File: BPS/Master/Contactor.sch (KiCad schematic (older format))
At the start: 20 parts, among them J7 ContactorConnector, Q1 VND5N07-E, Q2 NTR4003NT1G, U10 BAS70-04, U11 SI8261ABC-IS

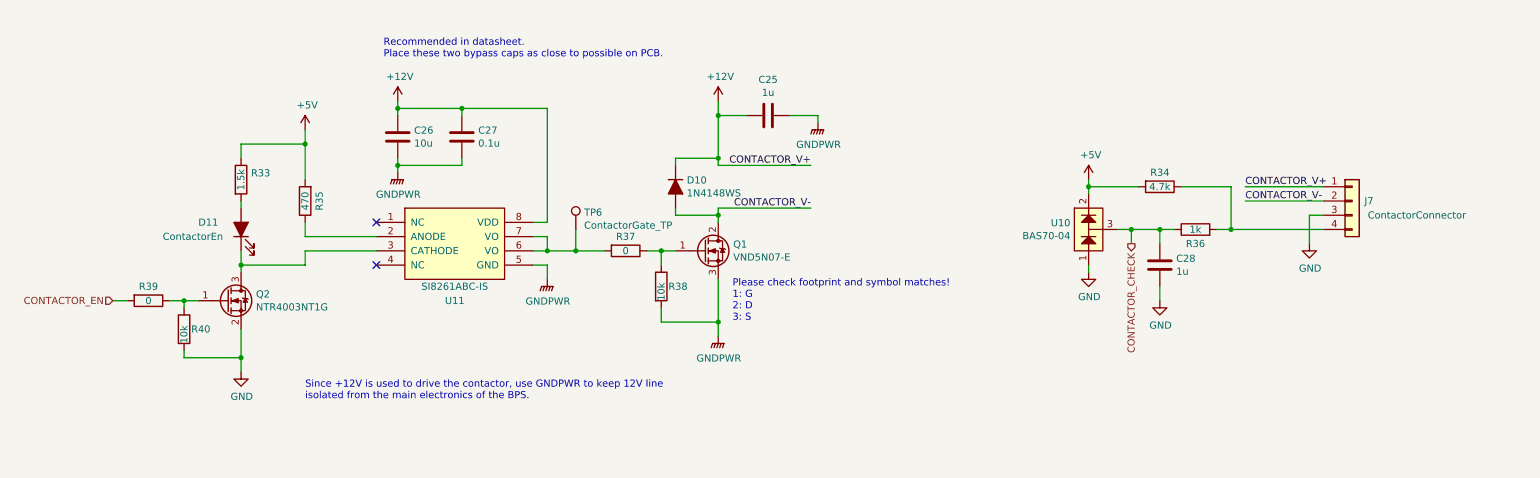
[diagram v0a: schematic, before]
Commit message: Creates fan brd interface schematics and updates symbols/footprints related to the leader board
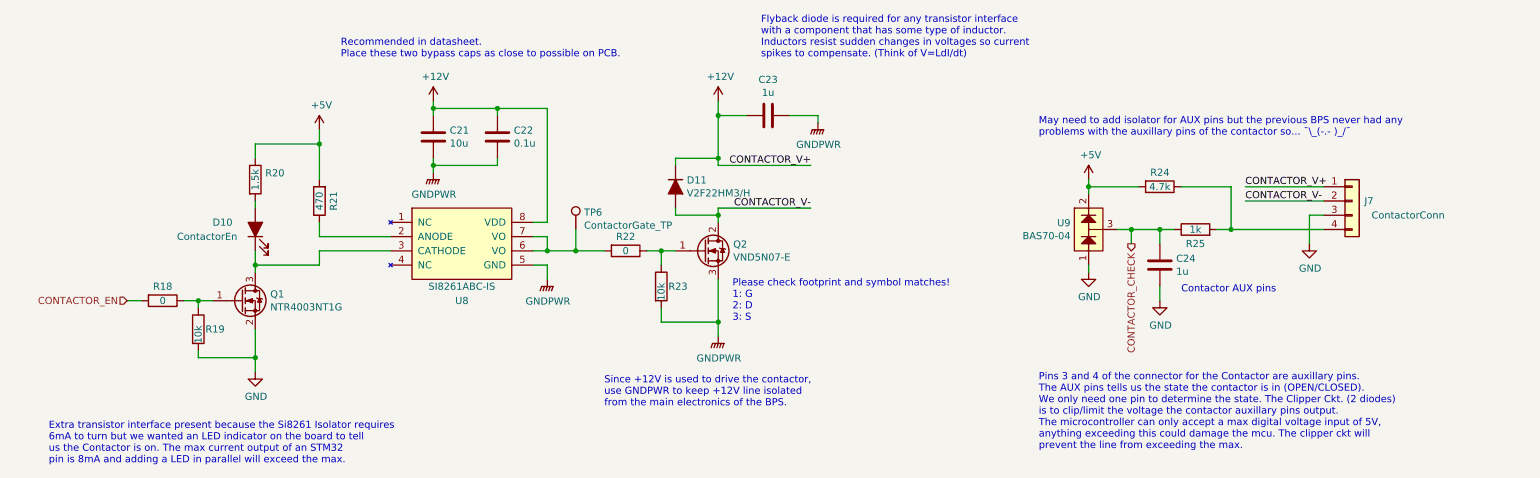
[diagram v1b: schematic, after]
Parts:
- removed U10: BAS70-04, Package_TO_SOT_SMD:SOT-23, symbol BPSMaster-rescue:BAS70-04-utsvt-bps
- removed U11: SI8261ABC-IS, Package_SO:SOIC-8_3.9x4.9mm_P1.27mm, symbol BPSMaster-rescue:SI8261ABC-IS-utsvt-bps
- added U8: SI8261ABC-IS, Package_SO:SOIC-8_3.9x4.9mm_P1.27mm, symbol utsvt-bps:SI8261ABC-IS
- added U9: BAS70-04, Package_TO_SOT_SMD:SOT-23, symbol utsvt-bps:BAS70-04
- D11: renamed from D10; value 1N4148WS -> V2F22HM3/H; footprint Diode_SMD:D_SOD-323 -> UTSVT_Passive:V2F22HM; Mouser (none) -> https://www.mouser.com/ProductDetail/Vishay-Semiconductors/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
- J7: value ContactorConnector -> ContactorConn
- renumbered C26 to C21, C27 to C22, C25 to C23, C28 to C24, D11 to D10, Q2 to Q1, Q1 to Q2, R39 to R18, R40 to R19, R33 to R20, R35 to R21, R37 to R22, R38 to R23, R34 to R24, R36 to R25
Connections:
- net +12V: now also U8.8 (VDD)
- net +5V: now also U9.2
- net CONTACTOR_CHECK: now also U9.3
- net GND: now also U9.1
- net GNDPWR: now also U8.5 (GND)
- net at R22.2, TP6.1: now also U8.6 (VO), U8.7 (VO)
- net at R21.1: now also U8.2 (ANODE)
- net at D10.1 (K), Q1.3 (D): now also U8.3 (CATHODE)
- no-connect marks 2 -> 0
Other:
- note added: "Contactor AUX pins"
- note added: "Extra transistor interface present because the Si8261 Isolator requires\n6mA to turn but we wanted an LED indicator on the board to tell\nus the Contactor is on. The max current output of an STM32\npin is 8mA and adding a LED in parallel will exceed the max."
- note added: "Flyback diode is required for any transistor interface\nwith a component that has some type of inductor.\nInductors resist sudden changes in voltages so current\nspikes to compensate. (Think of V=LdI/dt)"
- note added: "May need to add isolator for AUX pins but the previous BPS never had any\nproblems with the auxillary pins of the contactor so... ¯\_(-.- )_/¯"
- note added: "Pins 3 and 4 of the connector for the Contactor are auxillary pins.\nThe AUX pins tells us the state the contactor is in (OPEN/CLOSED).\nWe only need one pin to determine the state. The Clipper Ckt. (2 diodes)\nis to clip/limit the voltage the contactor auxillary pins output.\nThe microcontroller can only accept a max digital voltage input of 5V,\nanything exceeding this could damage the mcu. The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"
- note added: "Since +12V is used to drive the contactor,\nuse GNDPWR to keep +12V line isolated\nfrom the main electronics of the BPS."
- note removed: "Since +12V is used to drive the contactor, use GNDPWR to keep 12V line\nisolated from the main electronics of the BPS."
- moved on the sheet: C21, C22, D10, Q1, R18, R19, R20, R21

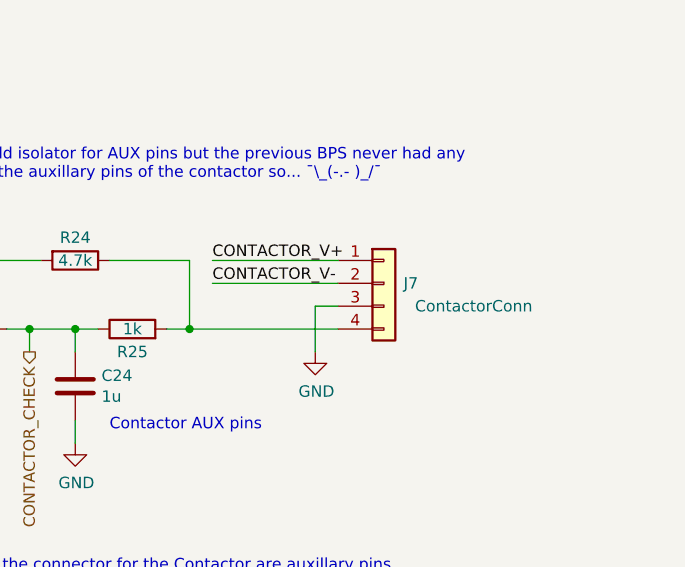
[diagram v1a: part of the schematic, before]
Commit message: Finishes schematics for bps leader board
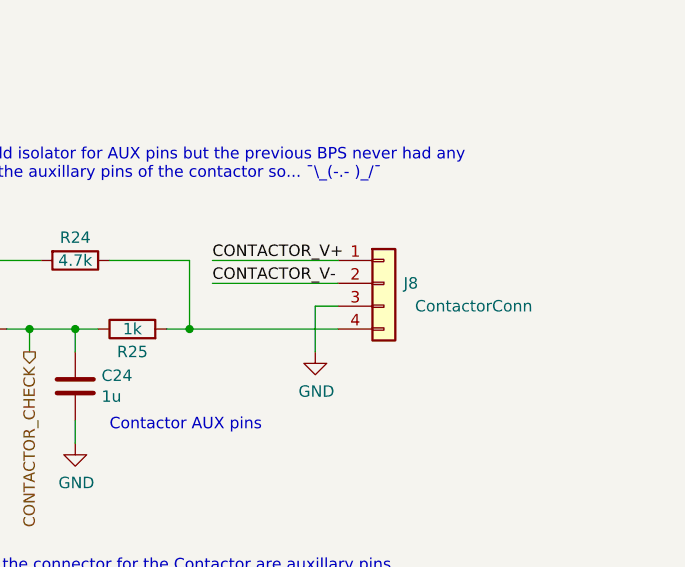
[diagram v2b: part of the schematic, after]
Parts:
- renumbered J7 to J8
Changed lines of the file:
@@
 $Descr A4 11693 8268
 encoding utf-8
-Sheet 6 10
+Sheet 6 11
 Title ""
 Date ""
@@
 $EndDescr
 $Comp
-L Connector_Generic:Conn_01x04 J7
+L Connector_Generic:Conn_01x04 J8
 U 1 1 5C2DA595
 P 10050 3500
-F 0 "J7" H 10200 3500 50  0000 R CNN
+F 0 "J8" H 10200 3500 50  0000 R CNN
 F 1 "ContactorConn" H 10700 3400 50  0000 R CNN
 F 2 "UTSVT_Connectors:Molex_MicroFit3.0_1x4xP3.00mm_PolarizingPeg_Vertical" H 10050 3500 50  0001 C CNN
@@
 $EndComp
 $Comp
-L power:GND #PWR059
+L power:GND #PWR062
 U 1 1 5C30292A
 P 9750 3800
-F 0 "#PWR059" H 9750 3550 50  0001 C CNN
+F 0 "#PWR062" H 9750 3550 50  0001 C CNN
 F 1 "GND" H 9755 3627 50  0000 C CNN
 F 2 "" H 9750 3800 50  0001 C CNN
@@
 	8700 4200 8700 4100
 $Comp
-L power:GND #PWR058
+L power:GND #PWR061
 U 1 1 5C304D16
 P 8700 4200
-F 0 "#PWR058" H 8700 3950 50  0001 C CNN
+F 0 "#PWR061" H 8700 3950 50  0001 C CNN
 F 1 "GND" H 8705 4027 50  0000 C CNN
 F 2 "" H 8700 4200 50  0001 C CNN
@@
 Connection ~ 8700 3700
 $Comp
-L power:GND #PWR057
+L power:GND #PWR060
 U 1 1 5C305432
 P 8200 4000
-F 0 "#PWR057" H 8200 3750 50  0001 C CNN
+F 0 "#PWR060" H 8200 3750 50  0001 C CNN
 F 1 "GND" H 8205 3827 50  0000 C CNN
 F 2 "" H 8200 4000 50  0001 C CNN
@@
 	8200 4000 8200 3950
 $Comp
-L power:+5V #PWR056
+L power:+5V #PWR059
 U 1 1 5C305723
 P 8200 3350
-F 0 "#PWR056" H 8200 3200 50  0001 C CNN
+F 0 "#PWR059" H 8200 3200 50  0001 C CNN
 F 1 "+5V" H 8215 3523 50  0000 C CNN
 F 2 "" H 8200 3350 50  0001 C CNN
@@
 Connection ~ 5200 3850
 $Comp
-L power:+12V #PWR050
+L power:+12V #PWR053
 U 1 1 5C30FC6C
 P 3600 2800
-F 0 "#PWR050" H 3600 2650 50  0001 C CNN
+F 0 "#PWR053" H 3600 2650 50  0001 C CNN
 F 1 "+12V" H 3615 2973 50  0000 C CNN
 F 2 "" H 3600 2800 50  0001 C CNN
@@
 	9200 3700 9100 3700
 $Comp
-L power:GNDPWR #PWR054
+L power:GNDPWR #PWR057
 U 1 1 5C3F7F9B
 P 5600 4450
-F 0 "#PWR054" H 5600 4250 50  0001 C CNN
+F 0 "#PWR057" H 5600 4250 50  0001 C CNN
 F 1 "GNDPWR" H 5604 4296 50  0000 C CNN
 F 2 "" H 5600 4400 50  0001 C CNN
@@
 $EndComp
 $Comp
-L power:GNDPWR #PWR051
+L power:GNDPWR #PWR054
 U 1 1 5C3F8405
 P 3600 3300
-F 0 "#PWR051" H 3600 3100 50  0001 C CNN
+F 0 "#PWR054" H 3600 3100 50  0001 C CNN
 F 1 "GNDPWR" H 3604 3146 50  0000 C CNN
 F 2 "" H 3600 3250 50  0001 C CNN
@@
 $EndComp
 $Comp
-L power:GNDPWR #PWR052
+L power:GNDPWR #PWR055
 U 1 1 5C3FD54A
 P 4400 4050
-F 0 "#PWR052" H 4400 3850 50  0001 C CNN
+F 0 "#PWR055" H 4400 3850 50  0001 C CNN
 F 1 "GNDPWR" H 4404 3896 50  0000 C CNN
 F 2 "" H 4400 4000 50  0001 C CNN
@@
 P 2350 4700
 AR Path="/5C392C6A/5C9B866F" Ref="#PWR?"  Part="1"
-AR Path="/5C38C674/5C9B866F" Ref="#PWR048"  Part="1"
-F 0 "#PWR048" H 2350 4450 50  0001 C CNN
+AR Path="/5C38C674/5C9B866F" Ref="#PWR051"  Part="1"
+F 0 "#PWR051" H 2350 4450 50  0001 C CNN
 F 1 "GND" H 2355 4527 50  0000 C CNN
 F 2 "" H 2350 4700 50  0001 C CNN
@@
 	2350 3950 2350 4000
 $Comp
-L power:+5V #PWR049
+L power:+5V #PWR052
 U 1 1 5C3C25EA
 P 2800 3000
-F 0 "#PWR049" H 2800 2850 50  0001 C CNN
+F 0 "#PWR052" H 2800 2850 50  0001 C CNN
 F 1 "+5V" H 2815 3173 50  0000 C CNN
 F 2 "" H 2800 3000 50  0001 C CNN
@@
 	4400 3850 4600 3850
 $Comp
-L power:+12V #PWR053
+L power:+12V #PWR056
 U 1 1 5C30CB9C
 P 5600 2800
-F 0 "#PWR053" H 5600 2650 50  0001 C CNN
+F 0 "#PWR056" H 5600 2650 50  0001 C CNN
 F 1 "+12V" H 5615 2973 50  0000 C CNN
 F 2 "" H 5600 2800 50  0001 C CNN
@@
 	6300 2950 6300 2900
 $Comp
-L power:GNDPWR #PWR055
+L power:GNDPWR #PWR058
 U 1 1 5C3F88F8
 P 6300 2950
-F 0 "#PWR055" H 6300 2750 50  0001 C CNN
+F 0 "#PWR058" H 6300 2750 50  0001 C CNN
 F 1 "GNDPWR" H 6304 2796 50  0000 C CNN
 F 2 "" H 6300 2900 50  0001 C CNN
